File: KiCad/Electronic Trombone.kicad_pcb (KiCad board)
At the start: 2 copper layers, 150 x 130 mm, 173 parts, among them J1 691137710002, J2 691137710003, J3 691137710003, J4 691137710002, J5 691137710002, J6 691137710002, Q1 NPN, Q2 PNP, Q3 NPN, Q4 PNP, Q5 NPN, Q6 NPN, SW1 D6R90F2LFS, SW2 D6R90F2LFS, SW3 D6R90F2LFS, SW4 SW_DPST, U1 CD74HC4051E, U10 TL074, U11 TL074, U2 TL074, U3 TL074, U4 40106, U5 TL074, U6 TL074, U7 TL074, U8 TL074, U9 TL074

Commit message: second checkpoint before complete redo of pcb
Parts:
- R10: footprint Resistor_SMD:R_0402_1005Metric -> Resistor_THT:R_Axial_DIN0207_L6.3mm_D2.5mm_P7.62mm_Horizontal
- moved SW4 22.7 mm to (113.8, 121.2), turned to 90 degrees
- moved R10 1.48 mm to (117.0, 108.3), turned to 90 degrees
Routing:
- net -9V: track 512.9 -> 64.9 mm, vias 8 -> 0
- net +9V: track 321.4 -> 108.6 mm
- net //Oscillator/Mix In 1: track 35.7 -> 2.54 mm
- net Net-(B1-Pad1): track 49.8 -> 30.8 mm
- net Net-(B2-Pad2): track 10.6 -> 22.3 mm
- net //Amp Control: track 14.1 -> 5.58 mm
- net Net-(U3A-+): track 19.4 -> 11.7 mm
- net //Buffered Audio Control: track 190.5 -> 195.1 mm, vias 0 -> 1
- net //Oscillator/Mix In 2: track 45.0 -> 47.1 mm
- net Net-(R10-Pad1): track 17.8 -> 19.9 mm
- net //Oscillator/Sch Inv Out 2: track 13.2 -> 13.8 mm

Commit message: Revert "second checkpoint before complete redo of pcb"
This reverts commit 4d5d4d4b5e4cbbcaee48991b351946aeae31b1e5.
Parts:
- R10: footprint Resistor_THT:R_Axial_DIN0207_L6.3mm_D2.5mm_P7.62mm_Horizontal -> Resistor_SMD:R_0402_1005Metric
- moved SW4 22.7 mm to (116.9, 143.7), turned to 0 degrees
- moved R10 1.48 mm to (118.5, 108.7), turned to 180 degrees
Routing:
- net -9V: track 64.9 -> 512.9 mm, vias 0 -> 8
- net +9V: track 108.6 -> 321.4 mm
- net //Oscillator/Mix In 1: track 2.54 -> 35.7 mm
- net Net-(B1-Pad1): track 30.8 -> 49.8 mm
- net Net-(B2-Pad2): track 22.3 -> 10.6 mm
- net //Amp Control: track 5.58 -> 14.1 mm
- net Net-(U3A-+): track 11.7 -> 19.4 mm
- net //Buffered Audio Control: track 195.1 -> 190.5 mm, vias 1 -> 0
- net //Oscillator/Mix In 2: track 47.1 -> 45.0 mm
- net Net-(R10-Pad1): track 19.9 -> 17.8 mm
- net //Oscillator/Sch Inv Out 2: track 13.8 -> 13.2 mm

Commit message: completed first draft
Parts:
- moved C30 32.6 mm to (148.3, 118.4)
- moved RV12 32.6 mm to (117.5, 71.6)
- moved C12 32.6 mm to (141.5, 49.6)
- moved C24 32.6 mm to (105.9, 49.5)
- moved C27 32.6 mm to (133.6, 85.8)
- moved C28 32.6 mm to (121.8, 109.8)
- moved C32 32.6 mm to (160.0, 87.4)
- moved C5 32.6 mm to (128.2, 33.1)
- moved C7 32.6 mm to (169.1, 38.7)
- moved C8 32.6 mm to (122.8, 66.5)
- moved C9 32.6 mm to (130.6, 126.6)
- moved D10 32.6 mm to (118.8, 82.8)
- moved D11 32.6 mm to (134.1, 83.6)
- moved D12 32.6 mm to (136.0, 115.8)
- moved D15 32.6 mm to (138.6, 108.2)
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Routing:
- net +9V: track 321.4 -> 420.3 mm, vias 1 -> 9
- net GND: track 0.00 -> 57.6 mm, vias 0 -> 44
- net -9V: track 512.9 -> 525.4 mm, vias 8 -> 13
- net Net-(Q1-B): track 0.00 -> 8.19 mm
- net //Oscillator/Mix In 1: track 35.7 -> 31.2 mm
- net Net-(B1-Pad1): track 49.8 -> 45.4 mm
- net Net-(U6C-+): track 9.11 -> 11.8 mm
- net /Power/Thaw 2: track 0.00 -> 2.54 mm
- net //Filter/Unprocessed Out: track 24.5 -> 22.1 mm
- net //Oscillator/Sch Inv Out 2: track 13.2 -> 12.2 mm
- net Net-(C4-Pad1): track 16.5 -> 17.6 mm
- net //Oscillator/Sch Inv In 1: track 37.3 -> 38.3 mm

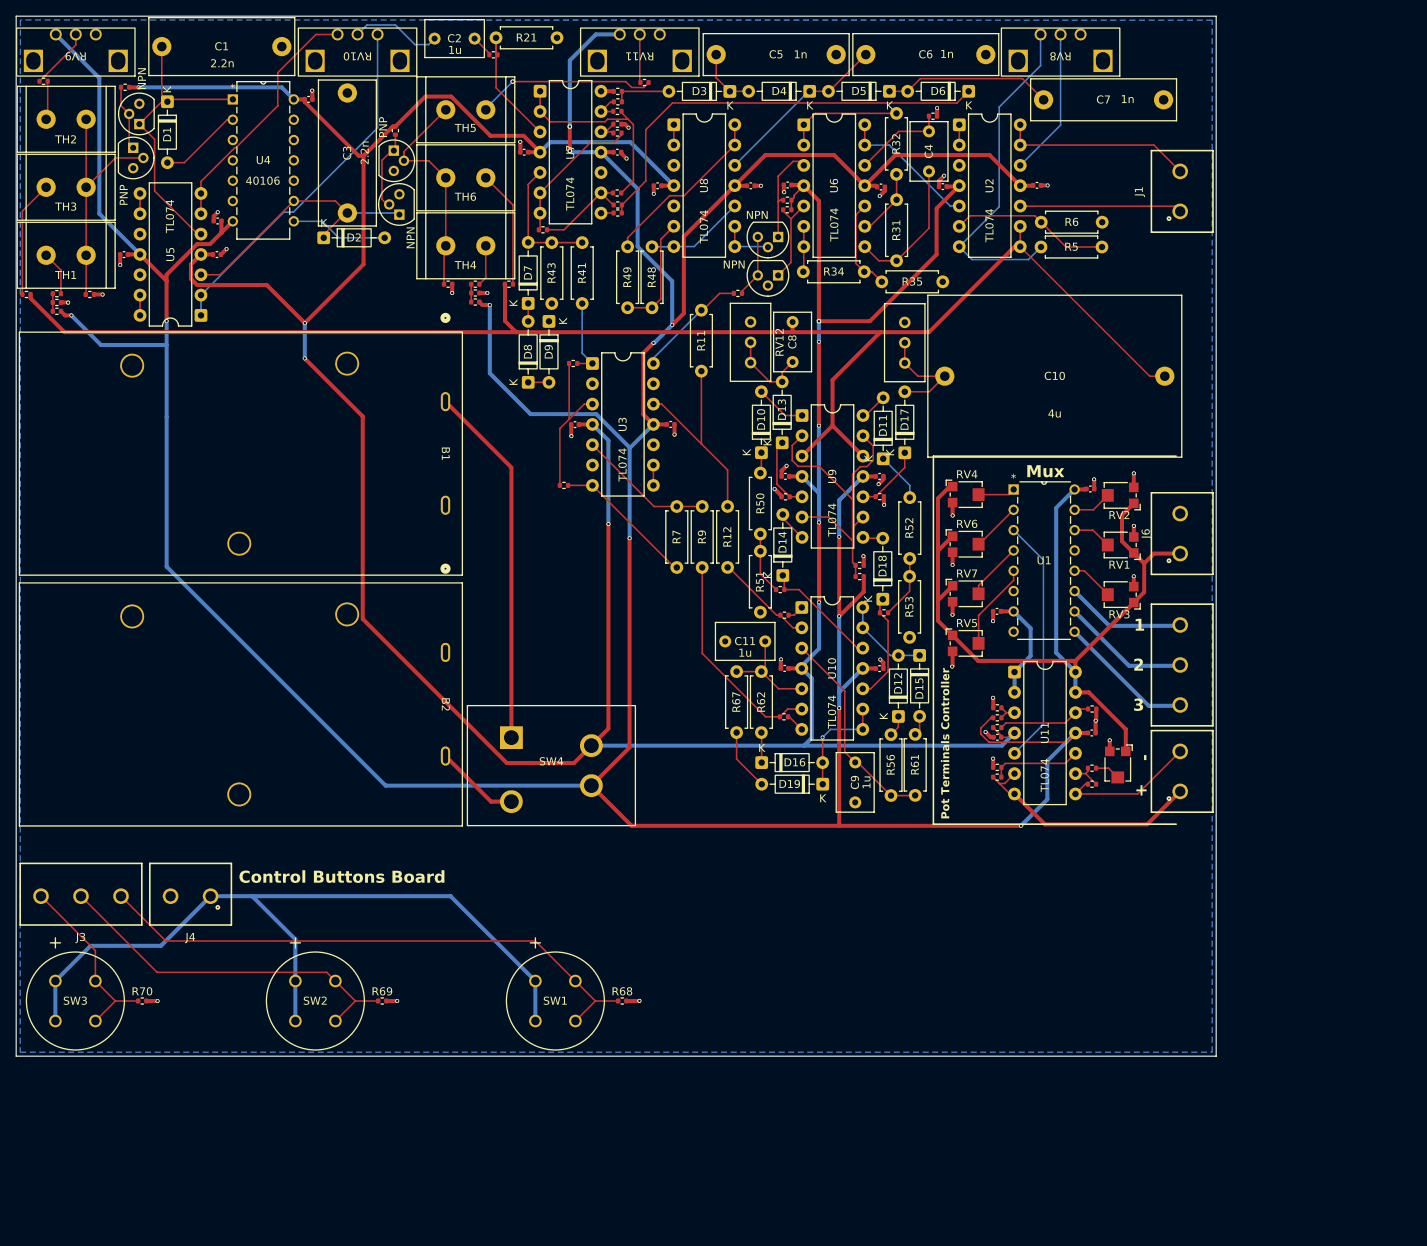
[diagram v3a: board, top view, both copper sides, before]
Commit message: all SMD are 0603 (imperial) now, started rerouting all traces
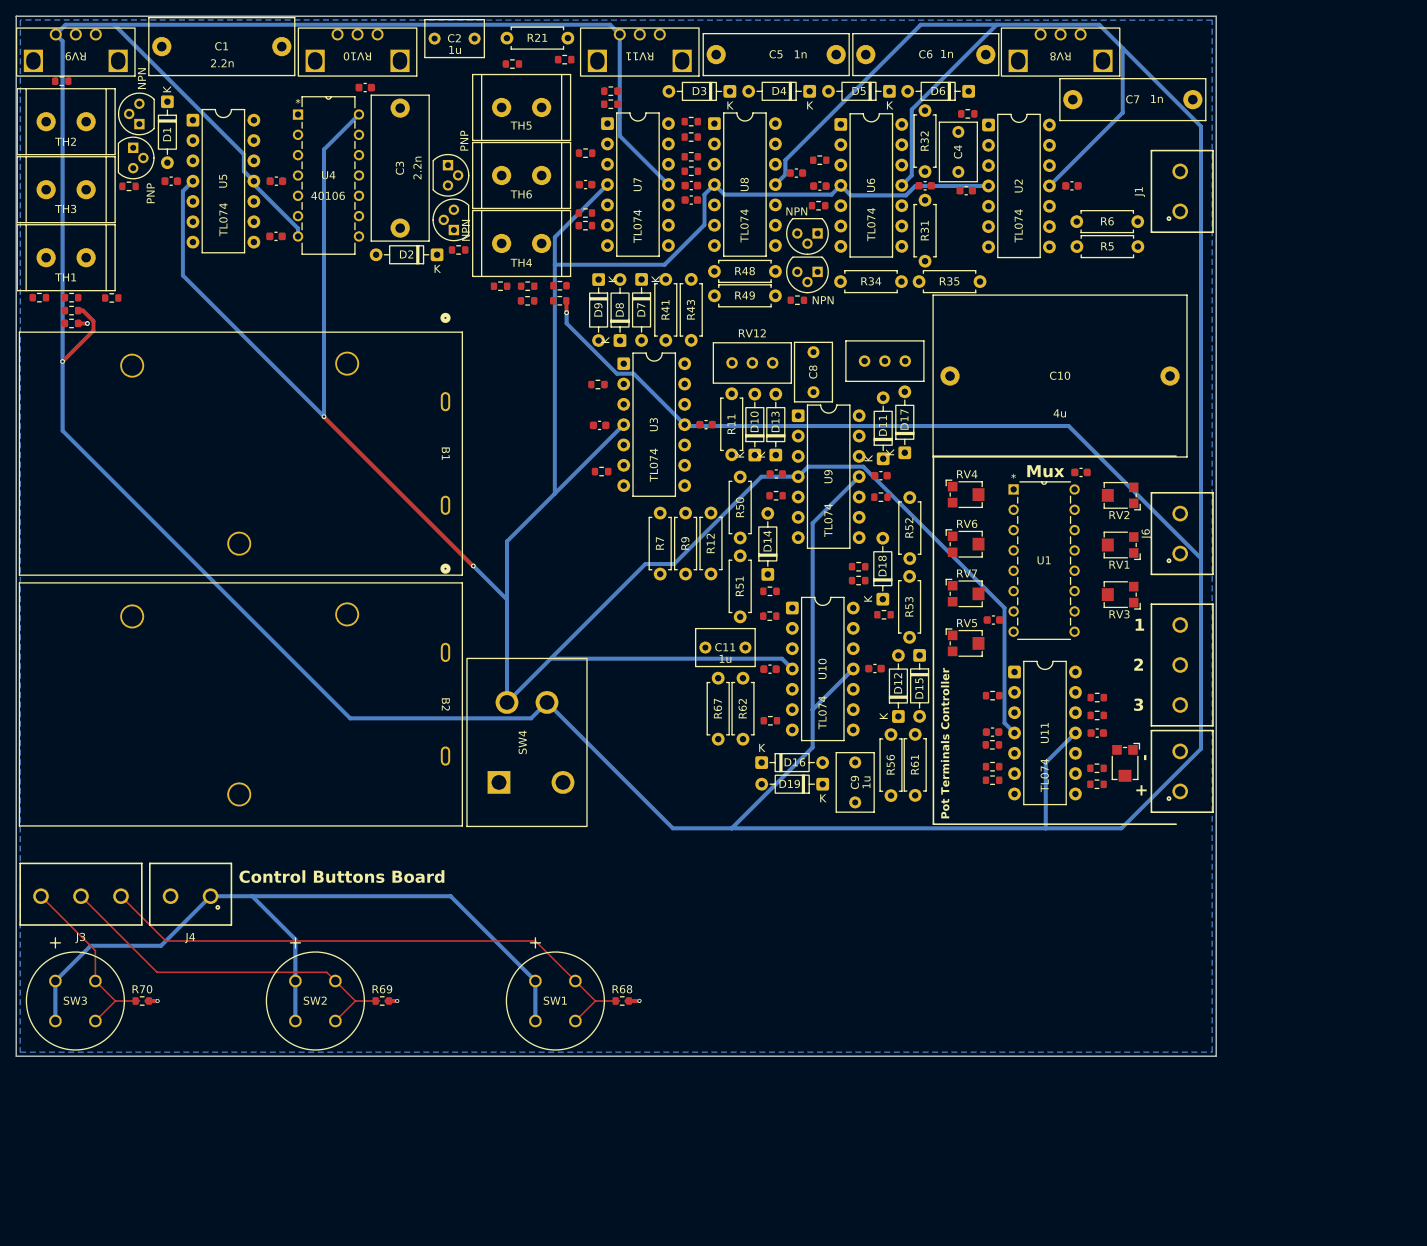
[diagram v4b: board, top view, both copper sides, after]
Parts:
- C12, C13, C14, C15, C16, C17, C18, C19, C20, C21, C22, C23, C24, C25, C26, C27, C28, C29, C30, C31, C32, C33: footprint Capacitor_SMD:C_0402_1005Metric -> Capacitor_SMD:C_0603_1608Metric
- R1, R10, R13, R14, R15, R16, R17, R18, R19, R2, R20, R22, R23, R24, R25, R26, R27, R28, R29, R3, R30, R33, R36, R37, R38, R39, R4, R40, R42, R44, R45, R46, R47, R54, R55, R58, R59, R60, R64, R65, R66, R68, R69, R70, R71, R72, R73, R74, R8: footprint Resistor_SMD:R_0402_1005Metric -> Resistor_SMD:R_0603_1608Metric
- moved U5 24.4 mm to (47.8, 41.3), turned to 0 degrees
- moved C19 21.1 mm to (58.2, 48.9), turned to 180 degrees
- moved R43 18.0 mm to (110.1, 68.8)
- moved R25 16.9 mm to (81.0, 57.5), turned to 180 degrees
- moved R48 16.1 mm to (120.6, 60.2), turned to 180 degrees
- moved R38 14.8 mm to (96.9, 54.5), turned to 0 degrees
- moved D7 14.5 mm to (103.9, 61.2), turned to -90 degrees
- moved D2 14.3 mm to (78.3, 58.1), turned to 180 degrees
- moved R44 14.3 mm to (100.0, 37.6)
- moved R46 13.6 mm to (100.0, 39.3)
- moved D8 12.6 mm to (101.2, 68.8)
- moved R73 12.5 mm to (160.8, 115.7)
- moved R49 12.5 mm to (113.0, 63.2), turned to 0 degrees
- moved R16 12.4 mm to (39.8, 49.5)
- moved R41 11.4 mm to (106.9, 61.2)
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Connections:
- R20 pad 2: Net-(U7A-+) -> Net-(U7B-+)
- R21 pad 2: Net-(U7A-+) -> Net-(U7B-+)
- R44 pad 1: Net-(U7C--) -> Net-(U7A--)
- R45 pad 2: Net-(U7C--) -> Net-(U7A--)
- R47 pad 2: Net-(U7C--) -> Net-(U7A--)
- U5 pad 1: //Oscillator/Mix In 2 -> /Power/Thaw 5C
- U5 pad 10: GND -> //Oscillator/Sch Inv In 2
- U5 pad 12: GND -> //Oscillator/Sch Inv In 1
- U5 pad 13: /Power/Thaw 5D -> //Oscillator/Mix In 1
- U5 pad 14: /Power/Thaw 5D -> //Oscillator/Mix In 1
- U5 pad 2: //Oscillator/Mix In 2 -> /Power/Thaw 5C
- U5 pad 3: //Oscillator/Sch Inv In 2 -> GND
- U5 pad 5: //Oscillator/Sch Inv In 1 -> GND
- U5 pad 6: //Oscillator/Mix In 1 -> /Power/Thaw 5D
- U5 pad 7: //Oscillator/Mix In 1 -> /Power/Thaw 5D
- U5 pad 8: /Power/Thaw 5C -> //Oscillator/Mix In 2
- U5 pad 9: /Power/Thaw 5C -> //Oscillator/Mix In 2
- U7 pad 1: //Filter/Signal In -> Net-(R46-Pad2)
- U7 pad 10: GND -> Net-(D7-A)
- U7 pad 2: //Filter/Signal In -> Net-(U7A--)
- U7 pad 3: Net-(U7A-+) -> GND
- U7 pad 5: Net-(D7-A) -> Net-(U7B-+)
- U7 pad 6: //Filter/Processed Control -> //Filter/Signal In
- U7 pad 7: //Filter/Processed Control -> //Filter/Signal In
- U7 pad 8: Net-(R46-Pad2) -> //Filter/Processed Control
- U7 pad 9: Net-(U7C--) -> //Filter/Processed Control
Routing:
- net //Buffered Audio Control: track 190.5 -> 0.00 mm
- net -9V: track 525.4 -> 713.5 mm, vias 13 -> 2
- net +5V: track 210.7 -> 96.6 mm
- net //Filter/Signal In w. -Offset: track 54.0 -> 0.00 mm
- net GND: track 57.6 -> 5.59 mm, vias 44 -> 4
- net Net-(B1-Pad1): track 45.4 -> 0.00 mm
- net //Oscillator/Mix In 2: track 45.0 -> 0.00 mm
- net //Envelope Generator/Trigger Ref: track 42.4 -> 0.00 mm
- net Net-(R5-Pad2): track 42.3 -> 0.00 mm
- net //Oscillator/Sch Inv In 1: track 38.3 -> 0.00 mm
- net +9V: track 420.3 -> 382.5 mm, vias 9 -> 2
- net //Oscillator/Sch Inv In 2: track 34.1 -> 0.00 mm
- net //Oscillator/Mix In 1: track 31.2 -> 0.00 mm
- net /Custom Potentiometer Controls/Mux Out: track 30.9 -> 0.00 mm
- net //Oscillator/Core In 1: track 30.6 -> 0.00 mm
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
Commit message: improved power routing
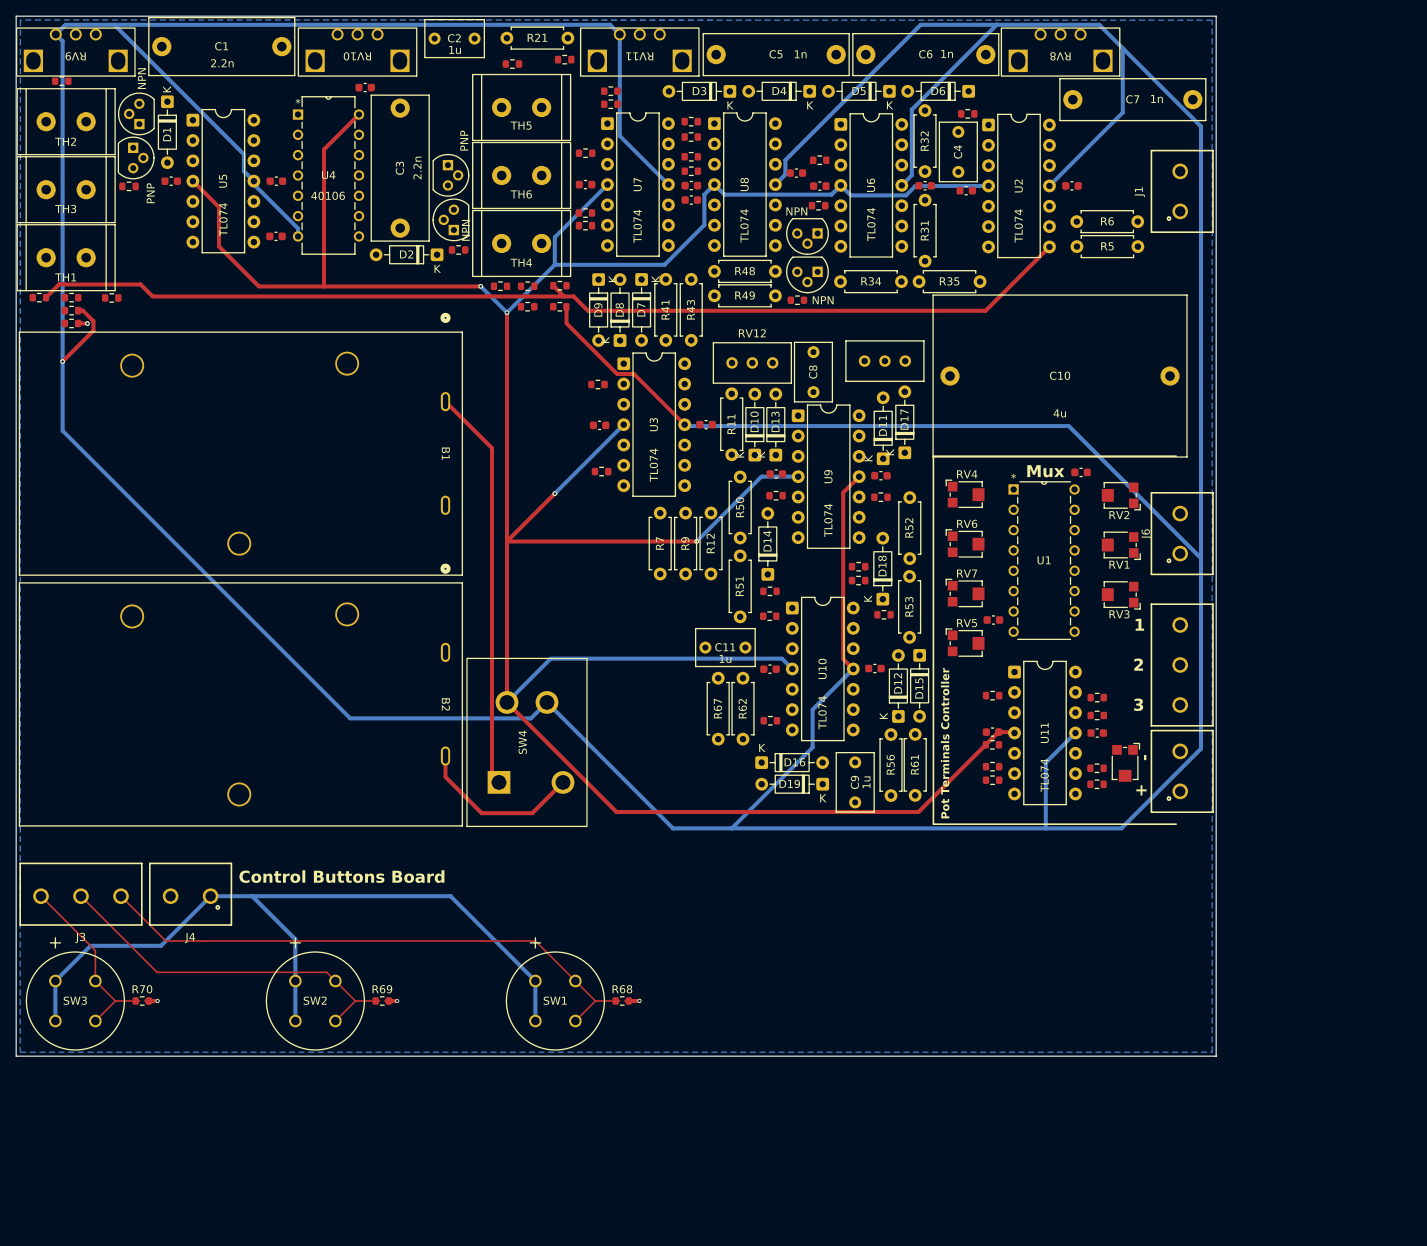
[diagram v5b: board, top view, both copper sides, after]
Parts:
- moved R24 0.75 mm to (93.7, 64.6)
- moved R22 0.73 mm to (89.6, 64.6)
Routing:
- net //Buffered Audio Control: track 0.00 -> 132.7 mm
- net Net-(B1-Pad1): track 0.00 -> 50.4 mm
- net Net-(B2-Pad2): track 0.00 -> 20.8 mm
- net -9V: track 713.5 -> 706.6 mm, vias 2 -> 1
- net +9V: track 382.5 -> 376.9 mm, vias 2 -> 4

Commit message: first JLCPCB order
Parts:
- moved R38 16.7 mm to (110.1, 44.2)
- moved R5 16.4 mm to (157.3, 43.1), turned to 0 degrees
- moved R74 15.1 mm to (147.7, 121.0), turned to 0 degrees
- moved D1 13.6 mm to (58.1, 39.0)
- moved R73 13.3 mm to (147.7, 113.2)
- moved R45 9.75 mm to (96.9, 43.1), turned to 180 degrees
- moved R18 9.26 mm to (37.6, 65.5)
- moved R6 7.70 mm to (164.9, 46.3)
- moved C11 2.79 mm to (109.3, 106.0), turned to -90 degrees
- moved R71 1.84 mm to (147.7, 111.4)
- moved C23 1.33 mm to (110.0, 52.6)
- moved R39 1.22 mm to (110.1, 40.2)
- moved R37 1.16 mm to (110.1, 42.2)
- moved R2 1.07 mm to (147.7, 124.8)
- moved R4 1.07 mm to (147.7, 123.2)
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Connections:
- R5 pad 1: Net-(U2B--) -> Net-(U2A--)
- R6 pad 2: Net-(U2B--) -> Net-(U2A--)
- U2 pad 1: /Power/Thaw 2 -> Net-(R5-Pad2)
- U2 pad 2: /Power/Thaw 2 -> Net-(U2A--)
- U2 pad 3: GND -> //Amplifier/Out
- U2 pad 5: //Amplifier/Out -> GND
- U2 pad 6: Net-(U2B--) -> /Power/Thaw 2
- U2 pad 7: Net-(R5-Pad2) -> /Power/Thaw 2
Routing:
- net +5V: track 96.6 -> 196.7 mm, vias 0 -> 1
- net GND: track 5.59 -> 74.3 mm, vias 4 -> 44
- net //Filter/Signal In w. -Offset: track 0.00 -> 46.4 mm
- net //Buffered Audio Control: track 132.7 -> 175.6 mm, vias 0 -> 3
- net +9V: track 376.9 -> 418.4 mm, vias 4 -> 9
- net //Oscillator/Sch Inv In 1: track 0.00 -> 41.1 mm
- net //Oscillator/Mix In 2: track 0.00 -> 37.3 mm, vias 0 -> 2
- net -9V: track 706.6 -> 743.4 mm, vias 1 -> 7
- net Net-(R5-Pad2): track 0.00 -> 36.6 mm
- net //Envelope Generator/Trigger Ref: track 0.00 -> 34.1 mm
- net //Oscillator/Sch Inv In 2: track 0.00 -> 32.5 mm
- net //Oscillator/Core In 1: track 0.00 -> 31.8 mm
- net /Custom Potentiometer Controls/+Pot: track 0.00 -> 30.9 mm
- net /Custom Potentiometer Controls/Mux Out: track 0.00 -> 29.8 mm
- net //Oscillator/Core In 2: track 0.00 -> 28.2 mm
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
